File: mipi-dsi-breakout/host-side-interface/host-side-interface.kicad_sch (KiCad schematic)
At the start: 13 parts, among them J2 Conn_01x03_Pin, J3 Conn_01x03_Pin, J4 Conn_01x03_Pin

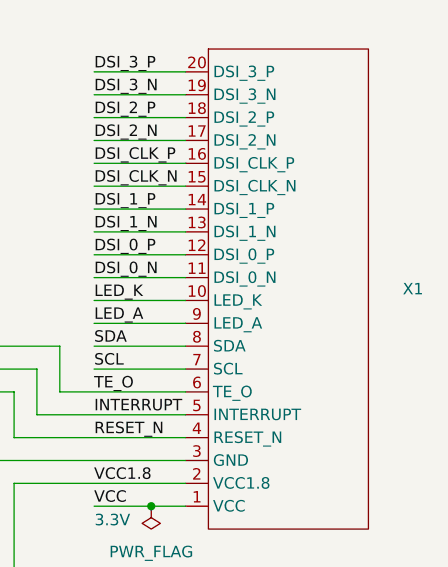
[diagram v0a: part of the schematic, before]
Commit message: Add two lcd screen connector symbols.
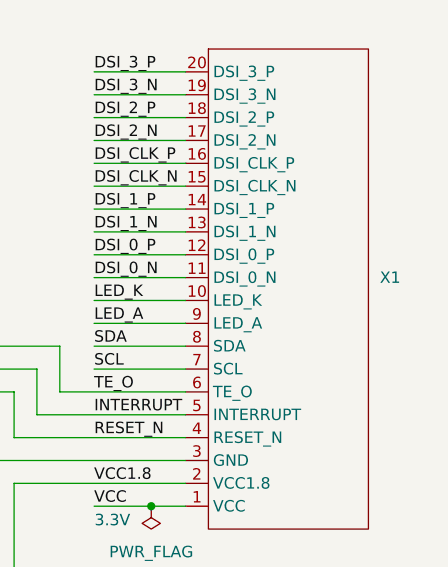
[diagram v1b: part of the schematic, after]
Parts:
- removed X1: ~, symbol project:mipi-breakout-header-conn
- added X1: ~, symbol project:mipi_breakout_header_conn
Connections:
- net DSI_0_N: now also X1.11 (DSI_0_N)
- net DSI_0_P: now also X1.12 (DSI_0_P)
- net DSI_1_N: now also X1.13 (DSI_1_N)
- net DSI_1_P: now also X1.14 (DSI_1_P)
- net DSI_2_N: now also X1.17 (DSI_2_N)
- net DSI_2_P: now also X1.18 (DSI_2_P)
- net DSI_3_N: now also X1.19 (DSI_3_N)
- net DSI_3_P: now also X1.20 (DSI_3_P)
- net DSI_CLK_N: now also X1.15 (DSI_CLK_N)
- net DSI_CLK_P: now also X1.16 (DSI_CLK_P)
- net GND: now also X1.3 (GND)
- net INTERRUPT: now also X1.5 (INTERRUPT)
- net LED_A: now also X1.9 (LED_A)
- net LED_K: now also X1.10 (LED_K)
- net RESET_N: now also X1.4 (RESET_N)
- net SCL: now also X1.7 (SCL)
- net SDA: now also X1.8 (SDA)
- net TE_O: now also X1.6 (TE_O)
- net VCC: now also X1.1 (VCC)
- net VCC1.8: now also X1.2 (VCC1.8)

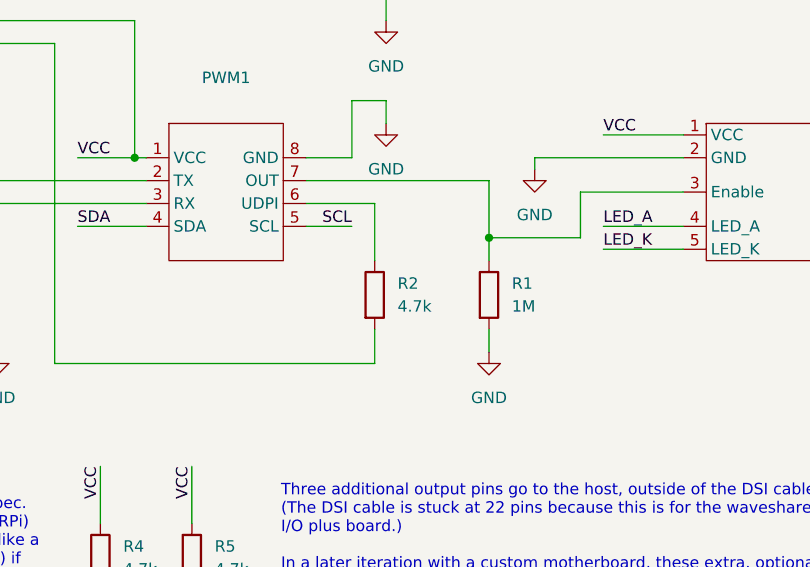
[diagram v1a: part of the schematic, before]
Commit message: Remove 4.7kOhm resistor from UDPI pin.
This should be part of the programmer PCB instead of the
host-side-interface.
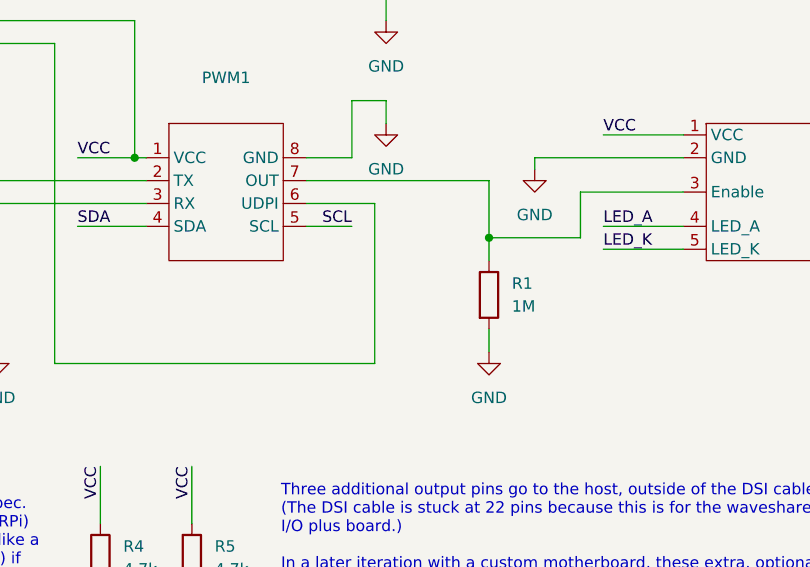
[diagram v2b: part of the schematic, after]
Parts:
- removed R2: 4.7k, symbol Device:R
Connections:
- net at J3.3 (Pin_3): now also PWM1.6 (UDPI)
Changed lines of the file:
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@@
 	(wire
 		(pts
-			(xy 154.94 71.12) (xy 154.94 77.47)
+			(xy 154.94 71.12) (xy 154.94 88.9)
 		)
 		(stroke
@@
 		(pts
 			(xy 212.09 115.57) (xy 144.78 115.57)
-		)
-		(stroke
-			(width 0)
-			(type default)
-		)
-	)
-	(wire
-		(pts
-			(xy 154.94 85.09) (xy 154.94 88.9)
 		)
 		(stroke
@@
 					(unit 1)
 				)
-			)
-		)
-	)
-	(symbol
-		(lib_id "Device:R")
-		(at 154.94 81.28 0)
-		(unit 1)
-		(exclude_from_sim no)
-		(in_bom yes)
-		(on_board yes)
-		(dnp no)
-		(fields_autoplaced yes)
-		(property "Reference" "R2"
-			(at 157.48 80.0099 0)
-			(effects
-				(font
-					(size 1.27 1.27)
-				)
-				(justify left)
-			)
-		)
-		(property "Value" "4.7k"
-			(at 157.48 82.5499 0)
-			(effects
-				(font
-					(size 1.27 1.27)
-				)
-				(justify left)
-			)
-		)
-		(property "Footprint" ""
-			(at 153.162 81.28 90)
-			(effects
-				(font
-					(size 1.27 1.27)
-				)
-				(hide yes)
-			)
-		)
-		(property "Datasheet" "~"
-			(at 154.94 81.28 0)
-			(effects
-				(font
-					(size 1.27 1.27)
-				)
-				(hide yes)
-			)
-		)
-		(property "Description" "Resistor"
-			(at 154.94 81.28 0)
-			(effects
-				(font
-					(size 1.27 1.27)
-				)
-				(hide yes)
-			)
-		)
-		(pin "1"
-		)
-		(pin "2"
-		)
-		(instances
-			(project ""
-				(path "/f2077993-b821-4408-bc59-2d0bd14a1026"
-					(reference "R2")
-					(unit 1)
-				)

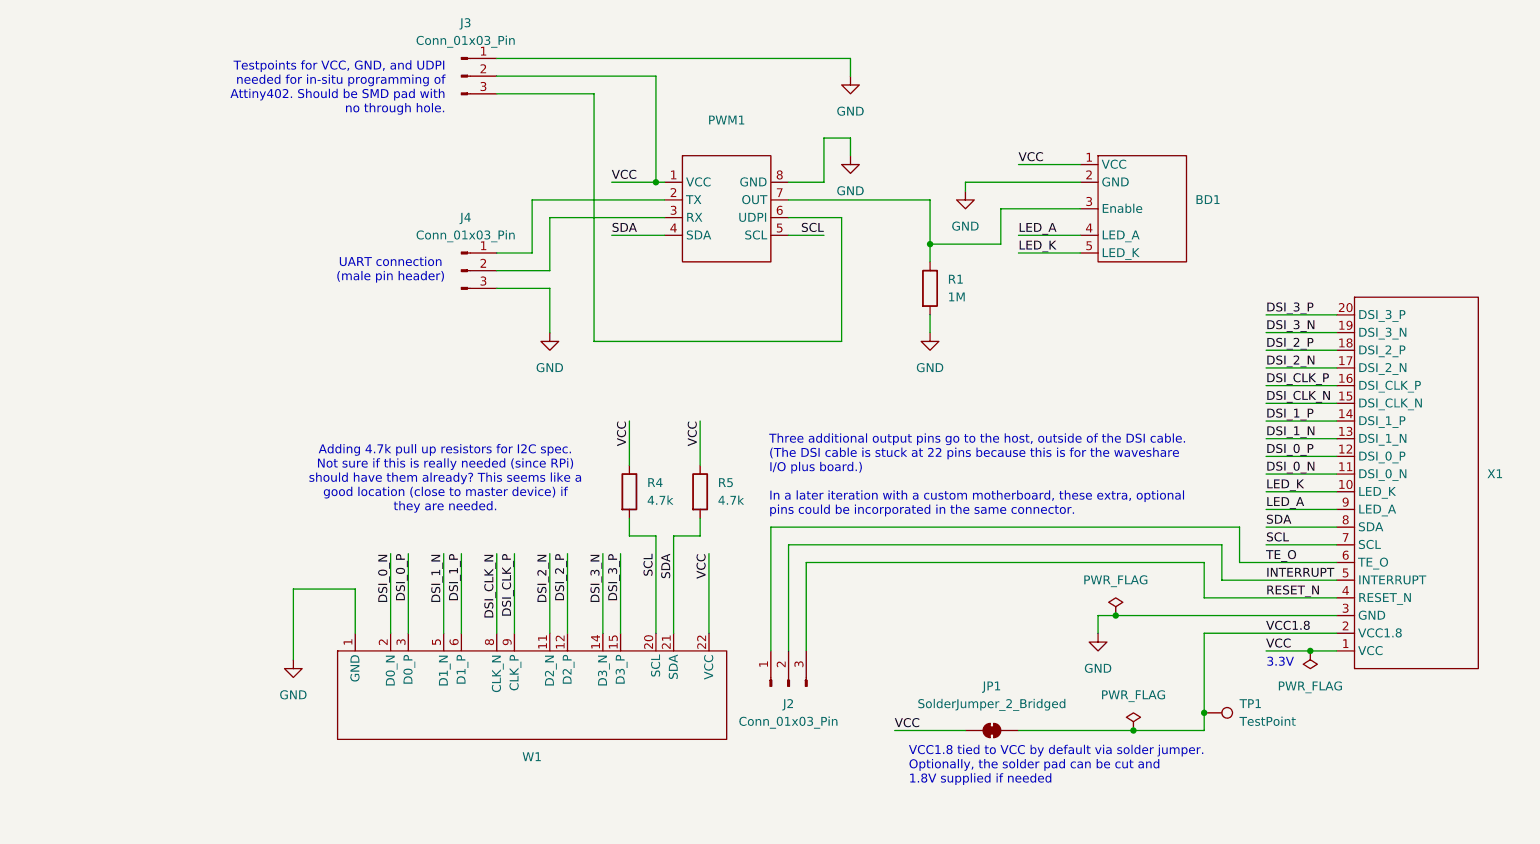
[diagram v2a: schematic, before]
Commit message: Replace BD1 part with AP5726 functional block schematic.
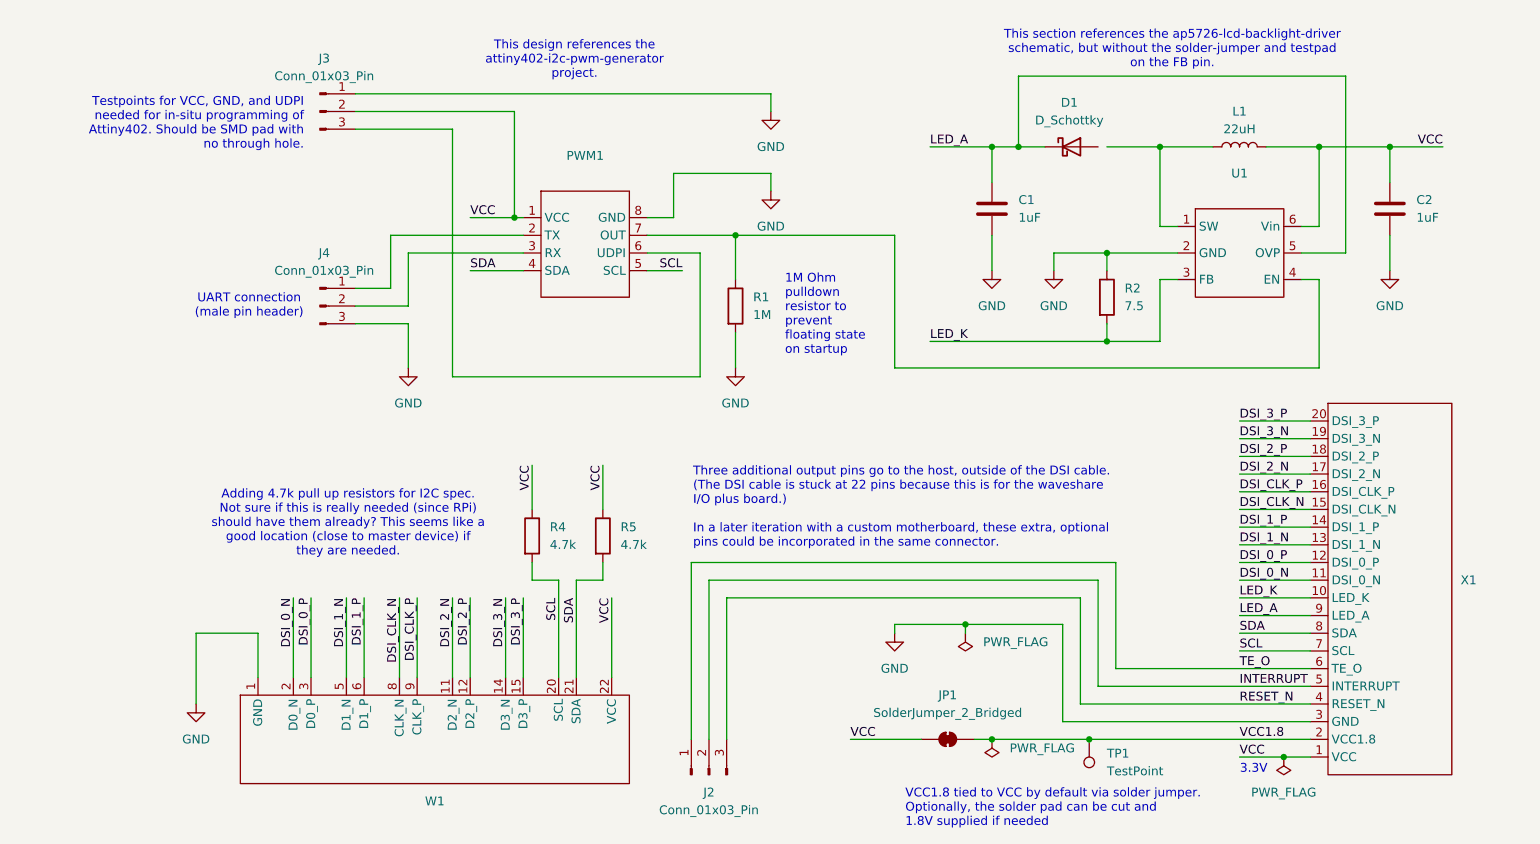
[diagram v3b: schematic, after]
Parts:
- removed BD1: ~, symbol project:backlight_driver
- added C1, C2: 1uF, symbol Device:C
- added D1: D_Schottky, symbol Device:D_Schottky
- added L1: 22uH, symbol Device:L
- added R2: 7.5, symbol Device:R
- added U1: ~, symbol project:ap5726
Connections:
- net GND: now also C1.2, C2.2, R2.1, U1.2 (GND)
- net LED_A: now also C1.1, D1.1 (K), U1.5 (OVP)
- net LED_K: now also R2.2, U1.3 (FB)
- net VCC: now also C2.1, L1.2, U1.6 (Vin)
- net at PWM1.7 (OUT), R1.1: now also U1.4 (EN)
- new net: L1.1, U1.1 (SW)
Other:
- note added: "1M Ohm pulldown resistor to prevent floating state on startup"
- note added: "This design references the attiny402-i2c-pwm-generator project."
- note added: "This section references the ap5726-lcd-backlight-driver schematic, but without the solder-jumper and testpad on the FB pin."
- moved on the sheet: J2, J3, J4, JP1, PWM1, R1, R4, R5, TP1, W1, X1
